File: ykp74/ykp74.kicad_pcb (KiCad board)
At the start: 2 copper layers, 100.7 x 76.7 mm, 22 parts, among them U1 27C256, U2 27C256, U3 27C256, U4 27C256, U5 74LS139, U6 74LS32, U7 74LS04, U8 74LS670

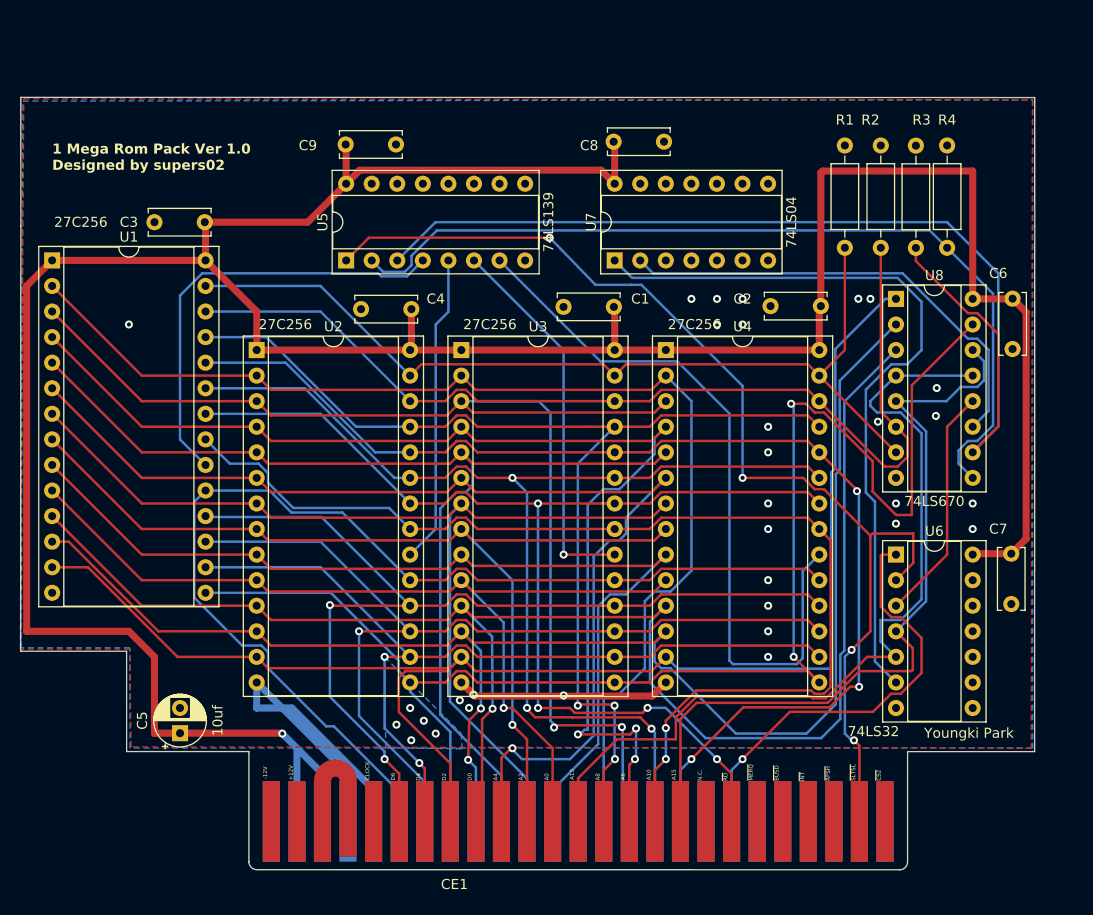
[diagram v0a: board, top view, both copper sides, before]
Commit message: Change the Foot Print of Edge slot
Signed-off-by: Youngki Park <ykp7409@gmail.com>
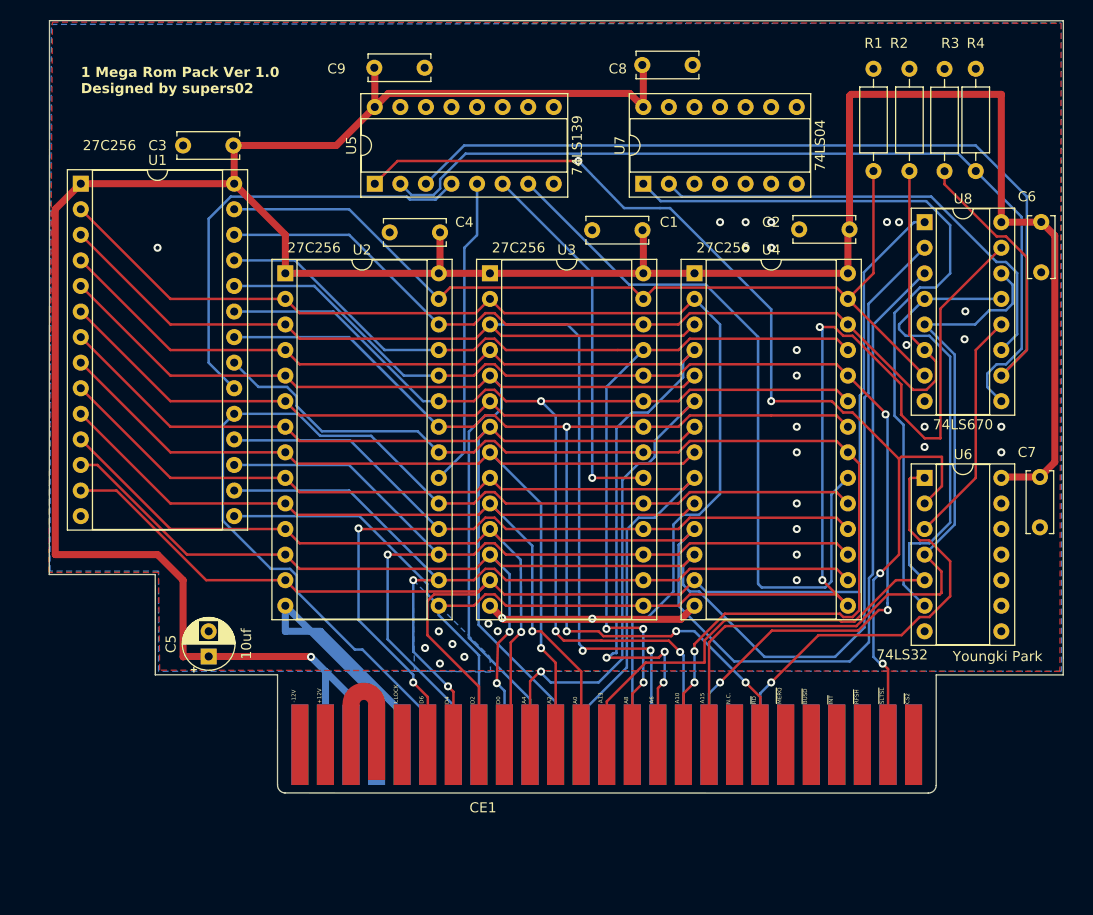
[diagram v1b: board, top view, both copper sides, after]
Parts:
- CE1: footprint ykp74_work_Library:card_edge_connector_MSX -> Lib_add:card_edge_connector_MSX
- moved C2 8.13 mm to (178.0, 79.5)
- moved C7 8.13 mm to (196.9, 104.1)
- moved R1 8.13 mm to (180.3, 63.5)
- moved R2 8.13 mm to (183.9, 73.7)
- moved R4 8.13 mm to (190.5, 73.7)
- moved U2 8.13 mm to (121.9, 83.8)
- moved U3 8.13 mm to (142.2, 83.8)
- moved U4 8.13 mm to (162.6, 83.8)
- moved U5 8.13 mm to (130.8, 74.9)
- moved U7 8.13 mm to (157.5, 74.9)
- moved C5 8.13 mm to (114.3, 121.9)
- moved C1 8.13 mm to (157.4, 79.5)
- moved U6 8.13 mm to (185.4, 104.1)
- moved U8 8.13 mm to (185.4, 78.7)
- moved C9 8.13 mm to (130.8, 63.4)
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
